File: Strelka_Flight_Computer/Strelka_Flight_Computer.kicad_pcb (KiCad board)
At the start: 4 copper layers, 91 x 30.1 mm, 165 parts, among them IC1 XTSD04GLGEAG, IC2 MAX-M10S-00B, J2 Conn_01x04, J3 DB125-3.5-4P-GN-S, J4 SM06B-GHS-TB(LF)(SN), J6 USB_B_Micro, J7 Conn_01x02, J8 Conn_01x07, Q1 CJK2333, Q10 AP2300, Q11 MMBT2222, Q15 AO3400A, Q16 AO3400A, Q17 AO3401A, Q2 CJK2333, Q4 AO3401A, Q5 AP2300, Q6 MMBT2222, Q9 AO3401A, SW1 SW_DIP_x01, SW6 TS-1185-C-A-A-A, SW7 TS-1185-C-A-A-A, U1 ASM330LHHXTR, U11 BMX055, U12 MS561101BA03-50, U16 TPS61085DGKR, U2 AP9101CK6, U3 AMS1117-3.3, U4 RFM95W-915S2, U5 MCP2551-I-SN, U6 STM32H743VITx, U8 USBLC6-2SC6, Y5 Q13FC1350000400, Y6 X1E0000210834

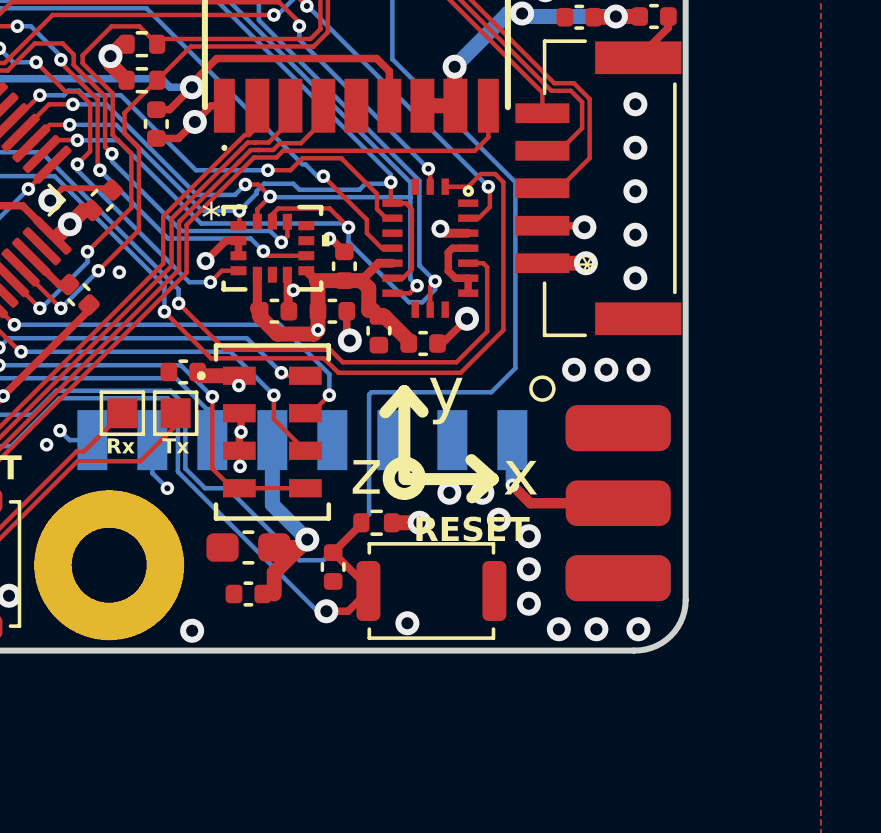
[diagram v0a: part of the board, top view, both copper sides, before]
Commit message: Adjusted changes after jlc tech team review
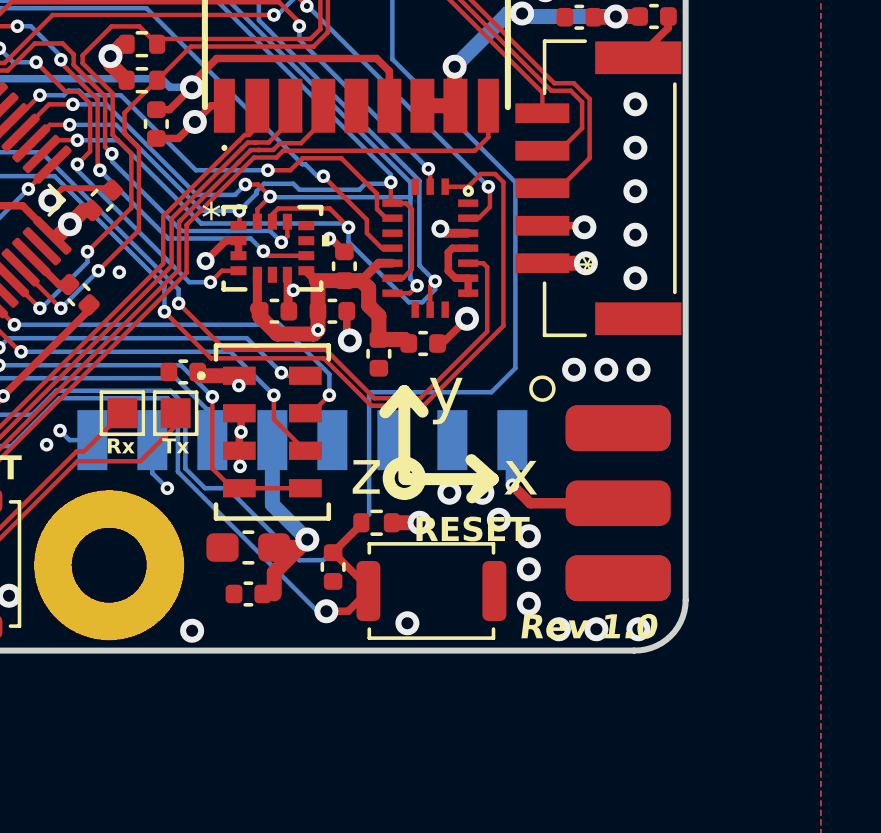
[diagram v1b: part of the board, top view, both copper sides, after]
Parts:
- moved C29 0.77 mm to (179.1, 68.5)
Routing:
- net /STM32H743/SPI2_NSS2: track 25.3 -> 26.3 mm
- net /STM32H743/SPI2_NSS3: track 32.1 -> 32.9 mm
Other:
- board text added: "Rev 1.0"
